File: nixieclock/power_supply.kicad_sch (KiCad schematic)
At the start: 44 parts, among them J1 USB_C_Receptacle, Q2 IRLR3110ZTRPBF, Q3 BSR92P, Q4 BSR92P, Q5 BSS131, Q6 BSS131, Q7 BSS131, Q8 BSS131, U1 LT3757AEMSE, U2 AMS1117-3.3

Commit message: finalized design ready for quality check
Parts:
- added D2, D3: LTST-C190GKT, LED_SMD:LED_0603_1608Metric_Pad1.05x0.95mm_HandSolder, symbol Device:LED_Small
- added R32: 3.3k, Resistor_SMD:R_0603_1608Metric_Pad1.05x0.95mm_HandSolder, symbol Device:R_Small
- added R33: 1.2k, Resistor_SMD:R_0603_1608Metric_Pad1.05x0.95mm_HandSolder, symbol Device:R_Small
- R3: value 140k -> 10k
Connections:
- net +3V3: now also D3.2 (A); no longer R3.1
- net GND: now also R3.1, R32.2, R33.2
- net VCC: now also D2.2 (A)
- new net: D3.1 (K), R33.1
- new net: D2.1 (K), R32.1
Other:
- note added: "3.3V_OK"
- note added: "VCC_OK"
- note removed: "TODO: - Add gate resistor on low-side NMOS - Add series resistors on gates"
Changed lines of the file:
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@@
   (title_block
     (title "Nixie Clock - Power Supply")
-    (date "2021-03-19")
+    (date "2021-03-24")
+    (rev "20210324")
     (company "Bastian de Byl")
     (comment 1 "https://github.com/tonyp7/170v-nixie-power-supply/")
@@
     (stroke (width 0) (type solid) (color 0 0 0 0))
   )
+  (wire (pts (xy 64.77 143.51) (xy 77.47 143.51))
+    (stroke (width 0) (type solid) (color 0 0 0 0))
+  )
   (wire (pts (xy 64.77 152.4) (xy 64.77 153.67))
     (stroke (width 0) (type solid) (color 0 0 0 0))
@@
     (stroke (width 0) (type solid) (color 0 0 0 0))
   )
+  (wire (pts (xy 77.47 143.51) (xy 77.47 144.78))
+    (stroke (width 0) (type solid) (color 0 0 0 0))
+  )
+  (wire (pts (xy 77.47 149.86) (xy 77.47 151.13))
+    (stroke (width 0) (type solid) (color 0 0 0 0))
+  )
+  (wire (pts (xy 77.47 156.21) (xy 77.47 157.48))
+    (stroke (width 0) (type solid) (color 0 0 0 0))
+  )
   (wire (pts (xy 80.01 71.12) (xy 80.01 72.39))
     (stroke (width 0) (type solid) (color 0 0 0 0))
@@
     (stroke (width 0) (type solid) (color 0 0 0 0))
   )
+  (wire (pts (xy 251.46 25.4) (xy 265.43 25.4))
+    (stroke (width 0) (type solid) (color 0 0 0 0))
+  )
   (wire (pts (xy 251.46 34.29) (xy 251.46 35.56))
+    (stroke (width 0) (type solid) (color 0 0 0 0))
+  )
+  (wire (pts (xy 265.43 25.4) (xy 265.43 26.67))
+    (stroke (width 0) (type solid) (color 0 0 0 0))
+  )
+  (wire (pts (xy 265.43 31.75) (xy 265.43 33.02))
+    (stroke (width 0) (type solid) (color 0 0 0 0))
+  )
+  (wire (pts (xy 265.43 38.1) (xy 265.43 39.37))
     (stroke (width 0) (type solid) (color 0 0 0 0))
   )
@@
     (effects (font (size 1.27 1.27)) (justify right bottom))
   )
+  (text "3.3V_OK" (at 87.63 144.78 180)
+    (effects (font (size 1.27 1.27) italic) (justify right bottom))
+  )
   (text "Neon Half Bridge" (at 104.775 104.775 0)
     (effects (font (size 1.27 1.27)) (justify left bottom))
@@
     (effects (font (size 1.27 1.27)) (justify right bottom))
   )
-  (text "TODO:\n- Add gate resistor on low-side NMOS\n- Add series resistors on gates"
-    (at 138.43 181.61 0)
-    (effects (font (size 1.27 1.27)) (justify left bottom))
-  )
   (text "200V" (at 147.32 35.56 180)
     (effects (font (size 1.27 1.27)) (justify right bottom))
@@
     (effects (font (size 1.27 1.27)) (justify left bottom))
   )
+  (text "VCC_OK" (at 275.59 26.67 180)
+    (effects (font (size 1.27 1.27) italic) (justify right bottom))
+  )
   (label "FBX" (at 80.01 66.04 180)
     (effects (font (size 1.27 1.27)) (justify right bottom))
@@
     (pin "1")
   )
-  (symbol (lib_id "power:+3.3V") (at 43.18 48.26 0) (unit 1)
-    (in_bom yes) (on_board yes)
-    (property "Reference" "#PWR012" (id 0) (at 43.18 52.07 0)
-      (effects (font (size 1.27 1.27)) hide)
-    )
-    (property "Value" "+3.3V" (id 1) (at 43.18 44.7126 0))
-    (property "Footprint" "" (id 2) (at 43.18 48.26 0)
-      (effects (font (size 1.27 1.27)) hide)
-    )
-    (property "Datasheet" "" (id 3) (at 43.18 48.26 0)
-      (effects (font (size 1.27 1.27)) hide)
-    )
-    (pin "1")
-  )
   (symbol (lib_id "power:+3.3V") (at 64.77 138.43 0) (unit 1)
     (in_bom yes) (on_board yes)
@@
     (pin "1")
   )
+  (symbol (lib_id "power:GND") (at 43.18 48.26 180) (unit 1)
+    (in_bom yes) (on_board yes)
+    (property "Reference" "#PWR0109" (id 0) (at 43.18 41.91 0)
+      (effects (font (size 1.27 1.27)) hide)
+    )
+    (property "Value" "GND" (id 1) (at 43.0657 43.9356 0))
+    (property "Footprint" "" (id 2) (at 43.18 48.26 0)
+      (effects (font (size 1.27 1.27)) hide)
+    )
+    (property "Datasheet" "" (id 3) (at 43.18 48.26 0)
+      (effects (font (size 1.27 1.27)) hide)
+    )
+    (pin "1")
+  )
   (symbol (lib_id "power:GND") (at 43.18 154.94 0) (unit 1)
     (in_bom yes) (on_board yes)
@@
     (pin "1")
   )
+  (symbol (lib_id "power:GND") (at 77.47 157.48 0) (unit 1)
+    (in_bom yes) (on_board yes)
+    (property "Reference" "#PWR012" (id 0) (at 77.47 163.83 0)
+      (effects (font (size 1.27 1.27)) hide)
+    )
+    (property "Value" "GND" (id 1) (at 77.5843 161.8044 0))
+    (property "Footprint" "" (id 2) (at 77.47 157.48 0)
+      (effects (font (size 1.27 1.27)) hide)
+    )
+    (property "Datasheet" "" (id 3) (at 77.47 157.48 0)
+      (effects (font (size 1.27 1.27)) hide)
+    )
+    (pin "1")
+  )
   (symbol (lib_id "power:GND") (at 100.33 72.39 0) (unit 1)
     (in_bom yes) (on_board yes)
@@
     (pin "1")
   )
+  (symbol (lib_id "power:GND") (at 265.43 39.37 0) (unit 1)
+    (in_bom yes) (on_board yes)
+    (property "Reference" "#PWR06" (id 0) (at 265.43 45.72 0)
+      (effects (font (size 1.27 1.27)) hide)
+    )
+    (property "Value" "GND" (id 1) (at 265.5443 43.6944 0))
+    (property "Footprint" "" (id 2) (at 265.43 39.37 0)
+      (effects (font (size 1.27 1.27)) hide)
+    )
+    (property "Datasheet" "" (id 3) (at 265.43 39.37 0)
+      (effects (font (size 1.27 1.27)) hide)
+    )
+    (pin "1")
+  )
   (symbol (lib_id "Personal:HV") (at 163.83 27.94 0) (unit 1)
     (in_bom yes) (on_board yes)
@@
     )
     (pin "1")
+  )
+  (symbol (lib_id "Device:R_Small") (at 77.47 153.67 0) (unit 1)
+    (in_bom yes) (on_board yes)
+    (property "Reference" "R33" (id 0) (at 78.9687 152.9091 0)
+      (effects (font (size 1.27 1.27)) (justify left))
+    )
+    (property "Value" "1.2k" (id 1) (at 78.9687 155.2078 0)
+      (effects (font (size 1.27 1.27)) (justify left))
+    )
+    (property "Footprint" "Resistor_SMD:R_0603_1608Metric_Pad1.05x0.95mm_HandSolder" (id 2) (at 77.47 153.67 0)
+      (effects (font (size 1.27 1.27)) hide)
+    )
+    (property "Datasheet" "~" (id 3) (at 77.47 153.67 0)
+      (effects (font (size 1.27 1.27)) hide)
+    )
+    (pin "1")
+    (pin "2")
   )
   (symbol (lib_id "Device:R_Small") (at 134.62 134.62 90) (unit 1)
@@
     )
     (property "Datasheet" "~" (id 3) (at 247.65 134.62 0)
+      (effects (font (size 1.27 1.27)) hide)
+    )
+    (pin "1")
+    (pin "2")
+  )
+  (symbol (lib_id "Device:R_Small") (at 265.43 35.56 0) (unit 1)
+    (in_bom yes) (on_board yes)
+    (property "Reference" "R32" (id 0) (at 266.9287 34.7991 0)
+      (effects (font (size 1.27 1.27)) (justify left))
+    )
+    (property "Value" "3.3k" (id 1) (at 266.9287 37.0978 0)
+      (effects (font (size 1.27 1.27)) (justify left))
+    )
+    (property "Footprint" "Resistor_SMD:R_0603_1608Metric_Pad1.05x0.95mm_HandSolder" (id 2) (at 265.43 35.56 0)
+      (effects (font (size 1.27 1.27)) hide)
+    )
+    (property "Datasheet" "~" (id 3) (at 265.43 35.56 0)
       (effects (font (size 1.27 1.27)) hide)
     )
@@
     (pin "2")
   )
+  (symbol (lib_id "Device:LED_Small") (at 77.47 147.32 90) (unit 1)
+    (in_bom yes) (on_board yes)
+    (property "Reference" "D3" (id 0) (at 79.1211 146.5591 90)
+      (effects (font (size 1.27 1.27)) (justify right))
+    )
+    (property "Value" "LTST-C190GKT" (id 1) (at 79.1211 148.8578 90)
+      (effects (font (size 1.27 1.27)) (justify right))
+    )
+    (property "Footprint" "LED_SMD:LED_0603_1608Metric_Pad1.05x0.95mm_HandSolder" (id 2) (at 77.47 147.32 90)
+      (effects (font (size 1.27 1.27)) hide)
+    )
+    (property "Datasheet" "~" (id 3) (at 77.47 147.32 90)
+      (effects (font (size 1.27 1.27)) hide)
+    )
+    (pin "1")
+    (pin "2")
+  )
+  (symbol (lib_id "Device:LED_Small") (at 265.43 29.21 90) (unit 1)
+    (in_bom yes) (on_board yes)
+    (property "Reference" "D2" (id 0) (at 267.0811 28.4491 90)
+      (effects (font (size 1.27 1.27)) (justify right))
+    )
+    (property "Value" "LTST-C190GKT" (id 1) (at 267.0811 30.7478 90)
+      (effects (font (size 1.27 1.27)) (justify right))
+    )
+    (property "Footprint" "LED_SMD:LED_0603_1608Metric_Pad1.05x0.95mm_HandSolder" (id 2) (at 265.43 29.21 90)
+      (effects (font (size 1.27 1.27)) hide)
+    )
+    (property "Datasheet" "~" (id 3) (at 265.43 29.21 90)
+      (effects (font (size 1.27 1.27)) hide)
+    )
+    (pin "1")
+    (pin "2")
+  )
   (symbol (lib_id "Device:R") (at 20.32 77.47 0) (unit 1)
     (in_bom yes) (on_board yes)
@@
       (effects (font (size 1.27 1.27)) (justify left))
     )
-    (property "Value" "140k" (id 1) (at 44.958 54.489 0)
+    (property "Value" "10k" (id 1) (at 44.958 54.489 0)
       (effects (font (size 1.27 1.27)) (justify left))
     )

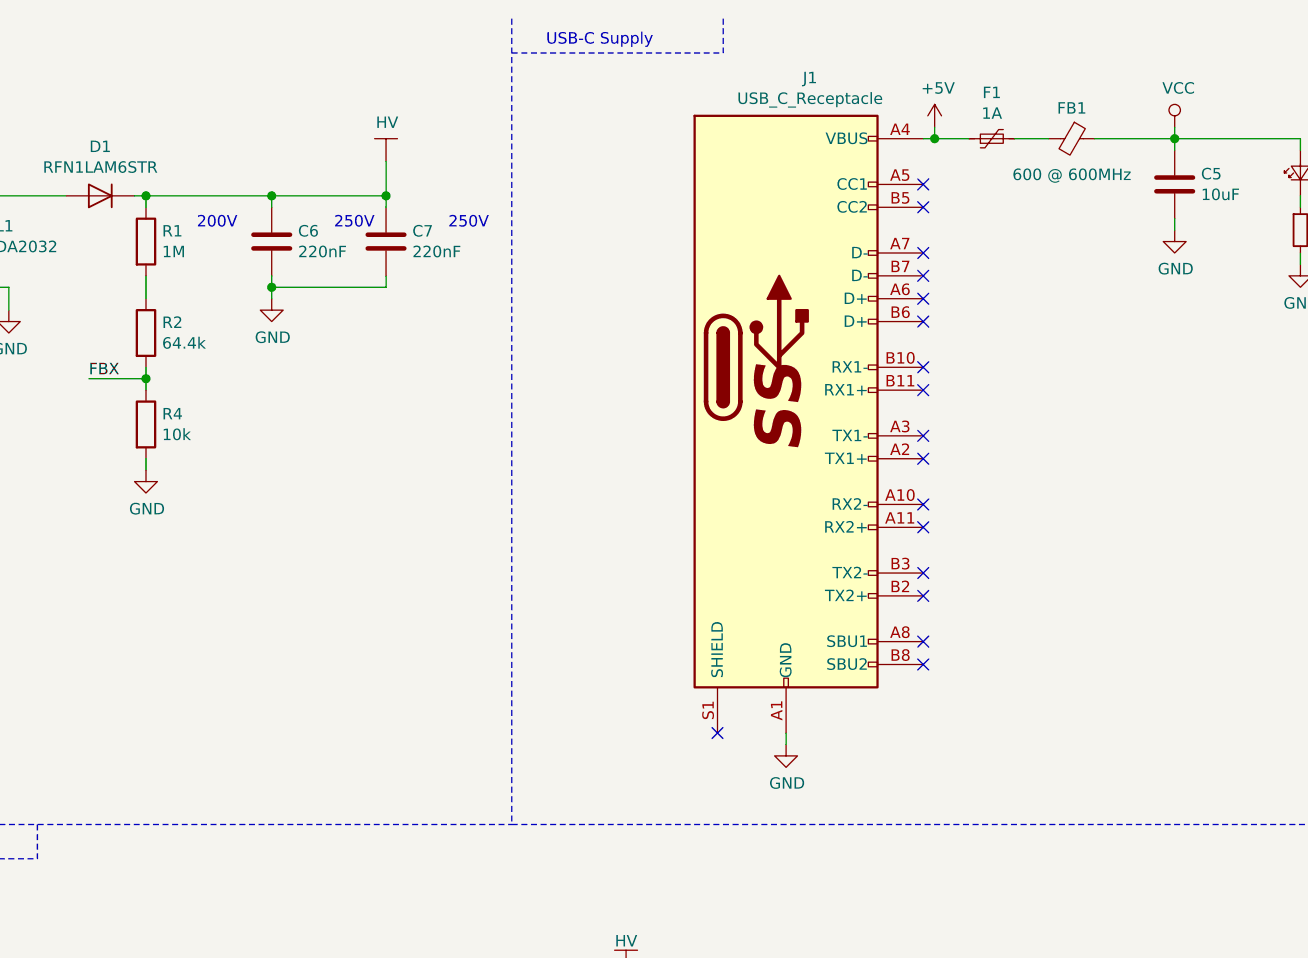
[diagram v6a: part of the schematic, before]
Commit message: finalized design, fixed USB C receptacle for hand soldering
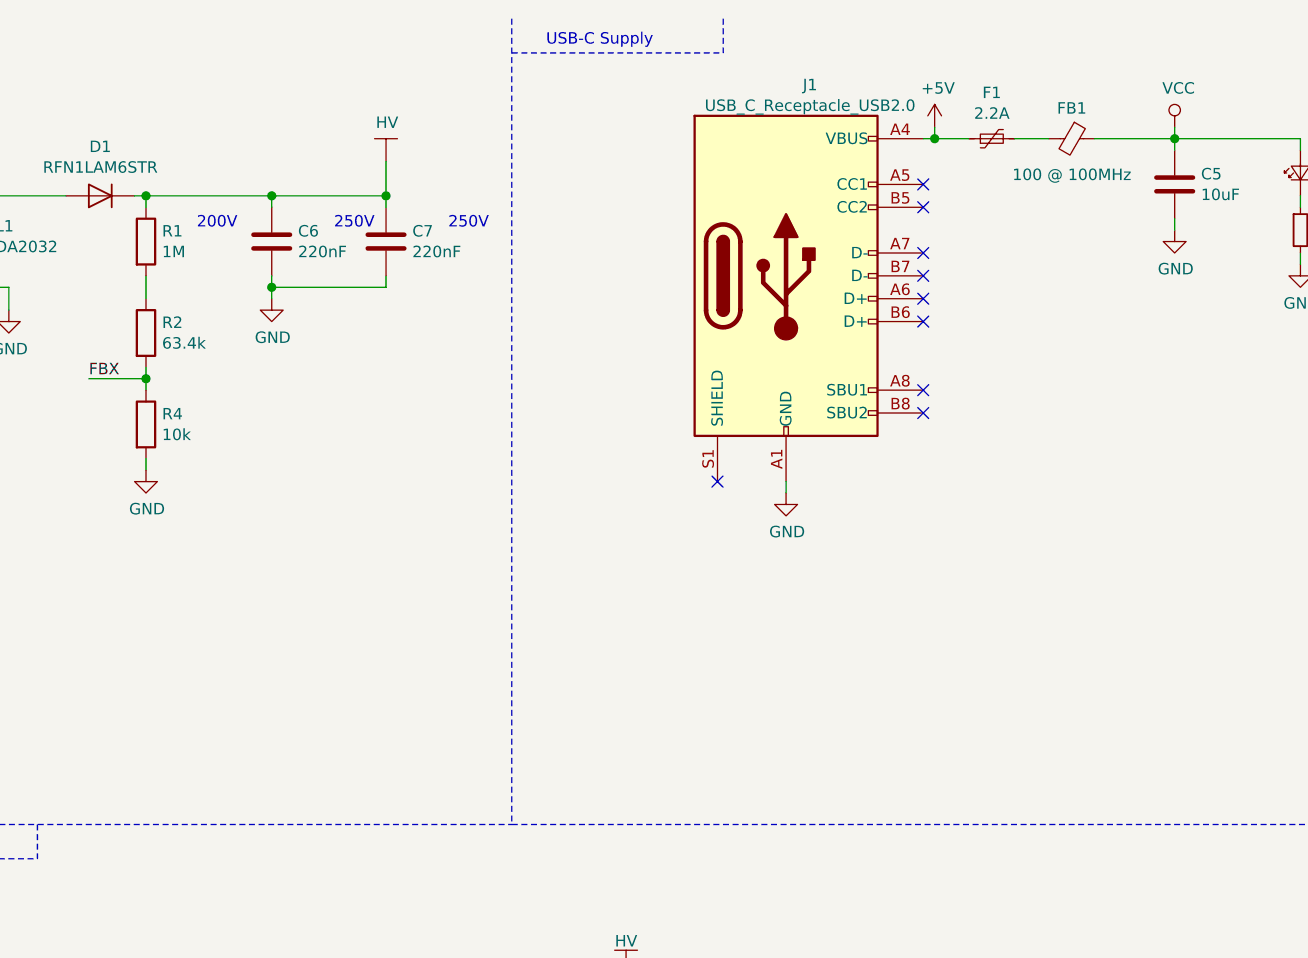
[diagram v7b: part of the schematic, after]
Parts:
- removed J1: USB_C_Receptacle, Connector_USB:USB_C_Receptacle_Amphenol_12401610E4-2A, symbol Connector:USB_C_Receptacle
- added J1: USB_C_Receptacle_USB2.0, Connector_USB:USB_C_Receptacle_GCT_USB4085, symbol Connector:USB_C_Receptacle_USB2.0
- C1, C2, C3, C4: footprint Capacitor_SMD:C_1210_3225Metric_Pad1.42x2.65mm_HandSolder -> Capacitor_SMD:C_1206_3216Metric_Pad1.42x1.75mm_HandSolder
- C5: footprint Capacitor_SMD:C_1206_3216Metric_Pad1.42x1.75mm_HandSolder -> Capacitor_SMD:C_0805_2012Metric_Pad1.15x1.40mm_HandSolder
- C9: footprint Capacitor_SMD:C_0603_1608Metric_Pad1.05x0.95mm_HandSolder -> Capacitor_SMD:C_0805_2012Metric_Pad1.15x1.40mm_HandSolder
- F1: value 1A -> 2.2A; footprint Fuse:Fuse_1206_3216Metric_Pad1.42x1.75mm_HandSolder -> Fuse:Fuse_1812_4532Metric_Pad1.30x3.40mm_HandSolder
- FB1: value 600 @ 600MHz -> 100 @ 100MHz
- R2: value 64.4k -> 63.4k
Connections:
- net +5V: now also J1.A4 (VBUS), J1.A9 (VBUS), J1.B4 (VBUS), J1.B9 (VBUS)
- net GND: now also J1.A1 (GND), J1.A12 (GND), J1.B1 (GND), J1.B12 (GND)
- no-connect marks 17 -> 9
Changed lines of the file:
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@@
     (rev "20210324")
     (company "Bastian de Byl")
-    (comment 1 "https://github.com/tonyp7/170v-nixie-power-supply/")
-    (comment 2 "Original HV source from 'tonyp7'")
+    (comment 1 "QC: OK")
+    (comment 3 "https://github.com/tonyp7/170v-nixie-power-supply/")
+    (comment 4 "Original HV source from 'tonyp7'")
   )
   (junction (at 25.4 25.4) (diameter 1.016) (color 0 0 0 0))
@@
   (junction (at 226.06 127) (diameter 1.016) (color 0 0 0 0))
   (junction (at 251.46 25.4) (diameter 1.016) (color 0 0 0 0))
-  (no_connect (at 200.66 91.44))
+  (no_connect (at 200.66 63.5))
   (no_connect (at 223.52 30.48))
   (no_connect (at 223.52 33.02))
@@
   (no_connect (at 223.52 43.18))
   (no_connect (at 223.52 45.72))
-  (no_connect (at 223.52 50.8))
   (no_connect (at 223.52 53.34))
-  (no_connect (at 223.52 58.42))
-  (no_connect (at 223.52 60.96))
-  (no_connect (at 223.52 66.04))
-  (no_connect (at 223.52 68.58))
-  (no_connect (at 223.52 73.66))
-  (no_connect (at 223.52 76.2))
-  (no_connect (at 223.52 81.28))
-  (no_connect (at 223.52 83.82))
+  (no_connect (at 223.52 55.88))
   (wire (pts (xy 20.32 63.5) (xy 20.32 73.66))
     (stroke (width 0) (type solid) (color 0 0 0 0))
@@
     (stroke (width 0) (type solid) (color 0 0 0 0))
   )
-  (wire (pts (xy 208.28 91.44) (xy 208.28 92.71))
+  (wire (pts (xy 208.28 63.5) (xy 208.28 64.77))
     (stroke (width 0) (type solid) (color 0 0 0 0))
   )
@@
     (pin "1")
   )
-  (symbol (lib_id "power:GND") (at 208.28 92.71 0) (unit 1)
-    (in_bom yes) (on_board yes)
-    (property "Reference" "#PWR017" (id 0) (at 208.28 99.06 0)
-      (effects (font (size 1.27 1.27)) hide)
-    )
-    (property "Value" "GND" (id 1) (at 208.3943 97.0344 0))
-    (property "Footprint" "" (id 2) (at 208.28 92.71 0)
-      (effects (font (size 1.27 1.27)) hide)
-    )
-    (property "Datasheet" "" (id 3) (at 208.28 92.71 0)
+  (symbol (lib_id "power:GND") (at 208.28 64.77 0) (unit 1)
+    (in_bom yes) (on_board yes)
+    (property "Reference" "#PWR017" (id 0) (at 208.28 71.12 0)
+      (effects (font (size 1.27 1.27)) hide)
+    )
+    (property "Value" "GND" (id 1) (at 208.3943 69.0944 0))
+    (property "Footprint" "" (id 2) (at 208.28 64.77 0)
+      (effects (font (size 1.27 1.27)) hide)
+    )
+    (property "Datasheet" "" (id 3) (at 208.28 64.77 0)
       (effects (font (size 1.27 1.27)) hide)
     )
@@
     (in_bom yes) (on_board yes)
     (property "Reference" "F1" (id 0) (at 231.14 20.3008 90))
-    (property "Value" "1A" (id 1) (at 231.14 22.6 90))
-    (property "Footprint" "Fuse:Fuse_1206_3216Metric_Pad1.42x1.75mm_HandSolder" (id 2) (at 236.22 24.13 0)
+    (property "Value" "2.2A" (id 1) (at 231.14 22.6 90))
+    (property "Footprint" "Fuse:Fuse_1812_4532Metric_Pad1.30x3.40mm_HandSolder" (id 2) (at 236.22 24.13 0)
       (effects (font (size 1.27 1.27)) (justify left) hide)
     )
-    (property "Datasheet" "~" (id 3) (at 231.14 25.4 0)
+    (property "Datasheet" "650-MINISMDC110F-2 " (id 3) (at 231.14 25.4 0)
       (effects (font (size 1.27 1.27)) hide)
     )
@@
       (effects (font (size 1.27 1.27)) (justify left))
     )
-    (property "Value" "64.4k" (id 1) (at 138.938 48.139 0)
+    (property "Value" "63.4k" (id 1) (at 138.938 48.139 0)
       (effects (font (size 1.27 1.27)) (justify left))
     )
@@
     (in_bom yes) (on_board yes)
     (property "Reference" "FB1" (id 0) (at 240.03 22.028 90))
-    (property "Value" "600 @ 600MHz" (id 1) (at 240.03 29.407 90))
+    (property "Value" "100 @ 100MHz" (id 1) (at 240.03 29.407 90))
     (property "Footprint" "Inductor_SMD:L_1206_3216Metric_Pad1.42x1.75mm_HandSolder" (id 2) (at 240.03 23.622 90)
       (effects (font (size 1.27 1.27)) hide)
     )
-    (property "Datasheet" "~" (id 3) (at 240.03 25.4 0)
+    (property "Datasheet" "710-742792118" (id 3) (at 240.03 25.4 0)
       (effects (font (size 1.27 1.27)) hide)
     )
@@
       (effects (font (size 1.27 1.27)) (justify left))
     )
-    (property "Footprint" "Capacitor_SMD:C_1210_3225Metric_Pad1.42x2.65mm_HandSolder" (id 2) (at 26.3652 34.29 0)
+    (property "Footprint" "Capacitor_SMD:C_1206_3216Metric_Pad1.42x1.75mm_HandSolder" (id 2) (at 26.3652 34.29 0)
       (effects (font (size 1.27 1.27)) hide)
     )
@@
       (effects (font (size 1.27 1.27)) (justify left))
     )
-    (property "Footprint" "Capacitor_SMD:C_1210_3225Metric_Pad1.42x2.65mm_HandSolder" (id 2) (at 37.7952 34.29 0)
+    (property "Footprint" "Capacitor_SMD:C_1206_3216Metric_Pad1.42x1.75mm_HandSolder" (id 2) (at 37.7952 34.29 0)
       (effects (font (size 1.27 1.27)) hide)
     )
@@
       (effects (font (size 1.27 1.27)) (justify left))
     )
-    (property "Footprint" "Capacitor_SMD:C_1210_3225Metric_Pad1.42x2.65mm_HandSolder" (id 2) (at 49.2252 34.29 0)
+    (property "Footprint" "Capacitor_SMD:C_1206_3216Metric_Pad1.42x1.75mm_HandSolder" (id 2) (at 49.2252 34.29 0)
       (effects (font (size 1.27 1.27)) hide)
     )
@@
       (effects (font (size 1.27 1.27)) (justify left))
     )
-    (property "Footprint" "Capacitor_SMD:C_1210_3225Metric_Pad1.42x2.65mm_HandSolder" (id 2) (at 60.6552 34.29 0)
+    (property "Footprint" "Capacitor_SMD:C_1206_3216Metric_Pad1.42x1.75mm_HandSolder" (id 2) (at 60.6552 34.29 0)
       (effects (font (size 1.27 1.27)) hide)
     )
@@
       (effects (font (size 1.27 1.27)) (justify left))
     )
-    (property "Footprint" "Capacitor_SMD:C_0603_1608Metric_Pad1.05x0.95mm_HandSolder" (id 2) (at 80.9752 80.01 0)
+    (property "Footprint" "Capacitor_SMD:C_0805_2012Metric_Pad1.15x1.40mm_HandSolder" (id 2) (at 80.9752 80.01 0)
       (effects (font (size 1.27 1.27)) hide)
     )
@@
       (effects (font (size 1.27 1.27)) (justify left))
     )
-    (property "Footprint" "Capacitor_SMD:C_1206_3216Metric_Pad1.42x1.75mm_HandSolder" (id 2) (at 252.4252 34.29 0)
+    (property "Footprint" "Capacitor_SMD:C_0805_2012Metric_Pad1.15x1.40mm_HandSolder" (id 2) (at 252.4252 34.29 0)
       (effects (font (size 1.27 1.27)) hide)
     )
@@
     (pin "9")
   )
-  (symbol (lib_id "Connector:USB_C_Receptacle") (at 208.28 50.8 0) (unit 1)
-    (in_bom yes) (on_board yes)
-    (property "Reference" "J1" (id 0) (at 210.947 18.6498 0))
-    (property "Value" "USB_C_Receptacle" (id 1) (at 210.947 20.9485 0))
-    (property "Footprint" "Connector_USB:USB_C_Receptacle_Amphenol_12401610E4-2A" (id 2) (at 212.09 50.8 0)
-      (effects (font (size 1.27 1.27)) hide)
-    )
-    (property "Datasheet" "https://www.usb.org/sites/default/files/documents/usb_type-c.zip" (id 3) (at 212.09 50.8 0)
+  (symbol (lib_id "Connector:USB_C_Receptacle_USB2.0") (at 208.28 40.64 0) (unit 1)
+    (in_bom yes) (on_board yes)
+    (property "Reference" "J1" (id 0) (at 210.947 19.4268 0))
+    (property "Value" "USB_C_Receptacle_USB2.0" (id 1) (at 210.947 21.7255 0))
+    (property "Footprint" "Connector_USB:USB_C_Receptacle_GCT_USB4085" (id 2) (at 212.09 40.64 0)
+      (effects (font (size 1.27 1.27)) hide)
+    )
+    (property "Datasheet" "https://www.digikey.com/en/products/detail/gct/USB4085-GF-A/9859662" (id 3) (at 212.09 40.64 0)
       (effects (font (size 1.27 1.27)) hide)
     )
     (pin "A1")
-    (pin "A10")
-    (pin "A11")
     (pin "A12")
-    (pin "A2")
-    (pin "A3")
     (pin "A4")
     (pin "A5")
@@
     (pin "A9")
     (pin "B1")
-    (pin "B10")
-    (pin "B11")
     (pin "B12")
-    (pin "B2")
-    (pin "B3")
     (pin "B4")
     (pin "B5")
